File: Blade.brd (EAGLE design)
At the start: 160 x 106.7 mm, 168 parts, among them IC1 THN10-2411WIR, IC10 MCP6064-E/SL, IC12 LM78L05ACMX/NOPB, IC13 CH340G, IC2 MCP6064-E/SL, IC3 MCP6064-E/SL, IC4 MCP6064-E/SL, IC5 MAX488CSA, IC6 MOCD207MSOIC-8, IC7 MOCD207MSOIC-8, IC8 MOCD207MSOIC-8, IC9 MCP6064-E/SL, Q1 12MHz, U1 ADR366WAUJZ, U10 ADS1148QPWRQ1, U11 ADS1148QPWRQ1, U12 ADS1148QPWRQ1, U13 ADR366WAUJZ, U2 ADR366WAUJZ, U3 ADS1148QPWRQ1, U4 ADS1148QPWRQ1, U5 ADS1148QPWRQ1, U6 LT1528, U7 S70FL01GS, U8 S70FL01GS, U9 STM32F77XXXLQFP208, X1 D-SUB9-H5M09RA, X2 D-SUB15-H5M15RA, X3 USBPTH

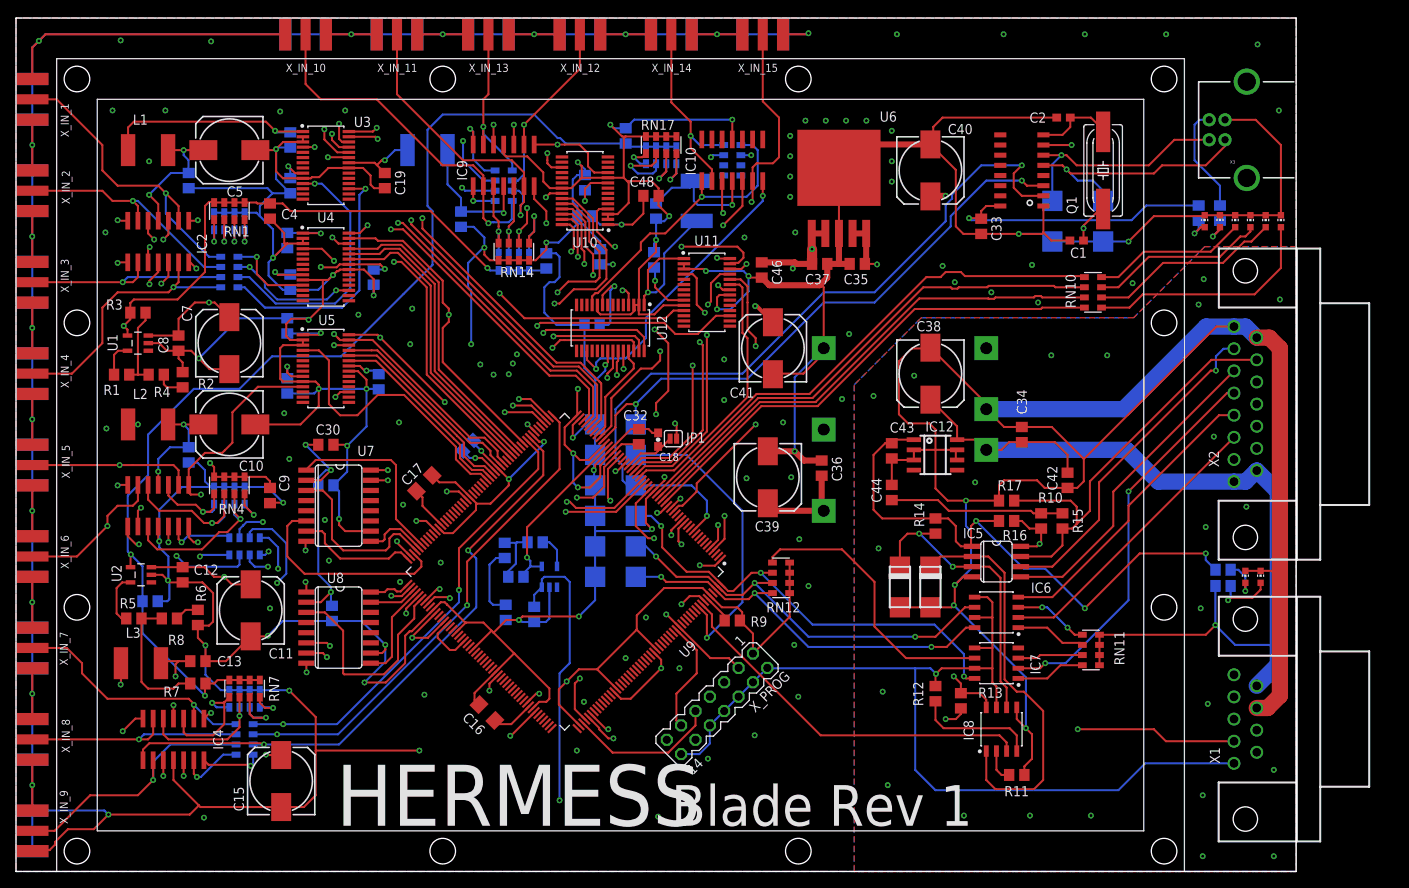
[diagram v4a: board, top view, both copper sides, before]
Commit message: interspu connector, ms select
interspu connector added
master/slave (solder)jumper added
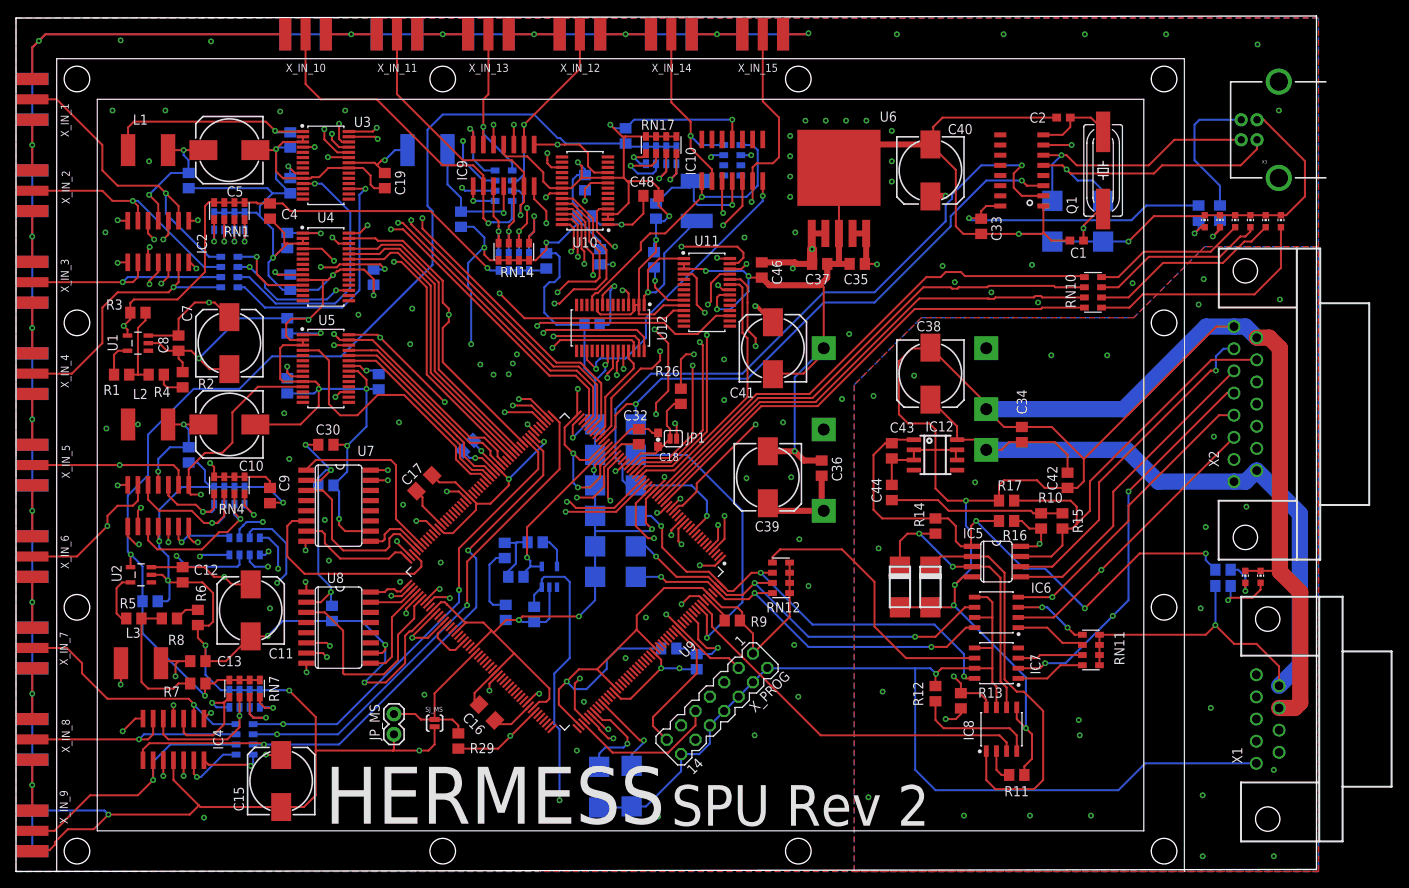
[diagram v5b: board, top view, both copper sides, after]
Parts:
- added D11, D12: 3V6, diodes:DMELF
- added JP_MS: (no value), aSparkFun:1X02
- added R26, R27, R29: 10k, rcl:R0805
- added R28: 99M, rcl:R0805
- added SJ_MS: (no value), aSparkFun:SJ_2S-NO
- D1, D2: value 3V6 -> 6V
- R12: value 3k -> 2k
- R13: value ~10k -> 4k7
- R14: value ~10k -> 7k5
- R9: value 20k -> 10k
- RN12: value 1k -> 300
- moved X3 4.00 mm to (155.1, 92.7)
- moved X1 2.79 mm to (156.5, 19.1)
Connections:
- net N$37 renamed PRD_ON
- removed net N$13: X_PROG.12
- removed net N$38: C18.1, JP1.1, U9.34
- removed net N$8: X_PROG.13
- new net 3V3CAP: U9.6
- new net INTERSPU_RX: D11.C, U9.166, X1.4
- new net INTERSPU_TX: D12.C, U9.163, X1.3
- new net MS_SEL: JP_MS.2, R29.1, SJ_MS.2, U9.129
- new net N$71: R27.1, R28.2, U9.197
- new net NRST: C18.1, JP1.1, R26.1, U9.34
- net 3V3: now also R26.2, R28.1, R29.2; no longer X1.2
- net GND: now also D11.A, D12.A, JP_MS.1, R27.2, SJ_MS.1
- net LO: now also X1.7
- net SODS: now also X1.5
- net SOE: now also X1.6
- net TCK: no longer X1.6
- net TDI: no longer X1.3
- net TDO: now also X_PROG.13; no longer X1.5, X_PROG.11
- net TMS: no longer X1.7
- net TRST: no longer X1.4
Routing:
- net INTERSPU_TX: track 0.00 -> 96.1 mm, vias 0 -> 2
- net INTERSPU_RX: track 0.00 -> 93.2 mm, vias 0 -> 2
- net TDI: track 116.0 -> 24.3 mm
- net TCK: track 105.7 -> 18.8 mm
- net TMS: track 103.9 -> 23.5 mm, vias 2 -> 1
- net TRST: track 116.9 -> 39.5 mm
- net TDO: track 89.1 -> 17.8 mm
- net SOE: track 37.5 -> 77.7 mm, vias 0 -> 1
- net LO: track 49.2 -> 77.3 mm, vias 2 -> 3
- net GND: track 1476.3 -> 1503.8 mm
- net SODS: track 36.3 -> 61.9 mm, vias 0 -> 1
- net MS_SEL: track 0.00 -> 20.2 mm
- net NRST: track 0.00 -> 12.7 mm
- net N$71: track 0.00 -> 12.1 mm, vias 0 -> 1
- net 5V: track 364.4 -> 373.0 mm
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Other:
- board size 160 x 106.7 mm -> 162.6 x 106.9 mm
- board text added: "SPU Rev 2"
- board text removed: "Blade Rev 1"
